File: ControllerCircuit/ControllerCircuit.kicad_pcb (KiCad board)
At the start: 2 copper layers, 122.5 x 87.5 mm, 91 parts, among them J1 ScrewTerminal, J10 Conn_01x02_Female, J11 Conn_01x03_Female, J12 ScrewTerminal, J13 Conn_01x02_Female, J2 ScrewTerminal3Pin, J3 ScrewTerminal3Pin, J4 ScrewTerminal, J5 ScrewTerminal, J6 AVR-ISP-6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

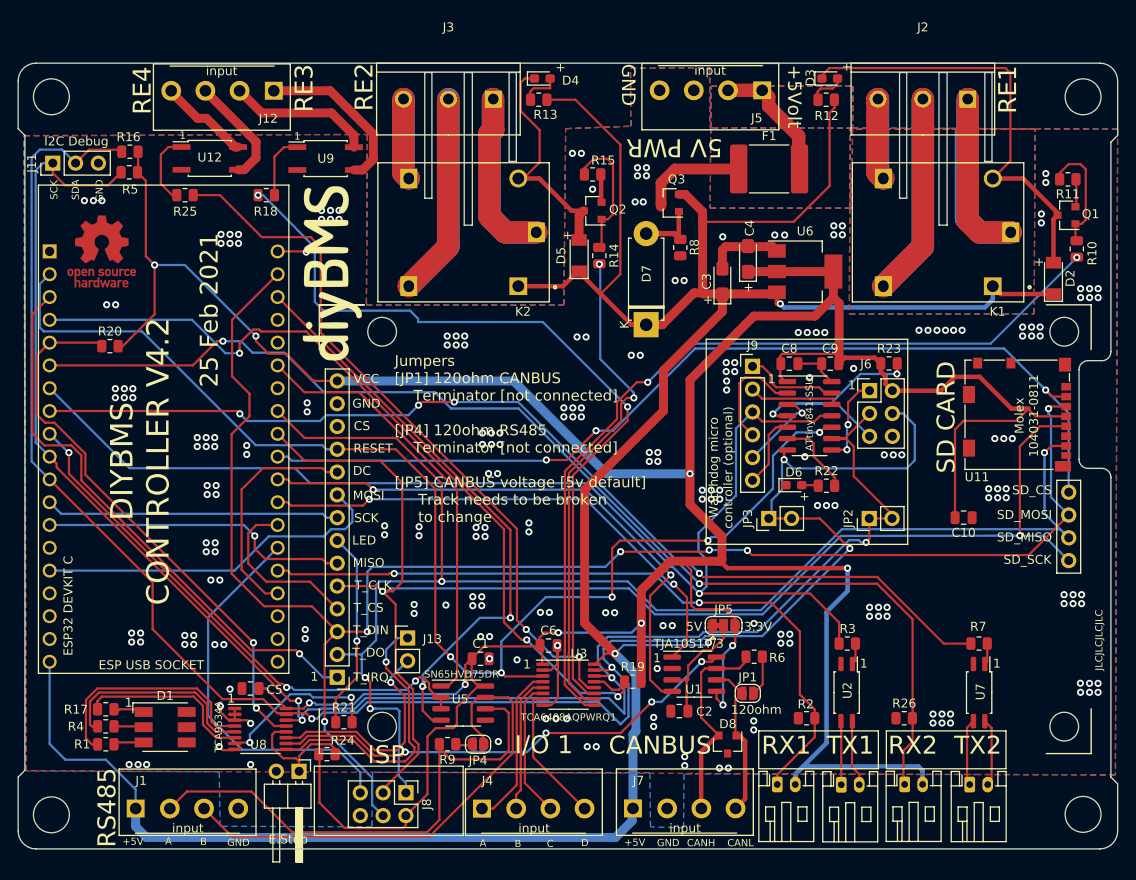
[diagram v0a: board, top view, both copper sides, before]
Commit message: Add pull up to J13 for remote touch display
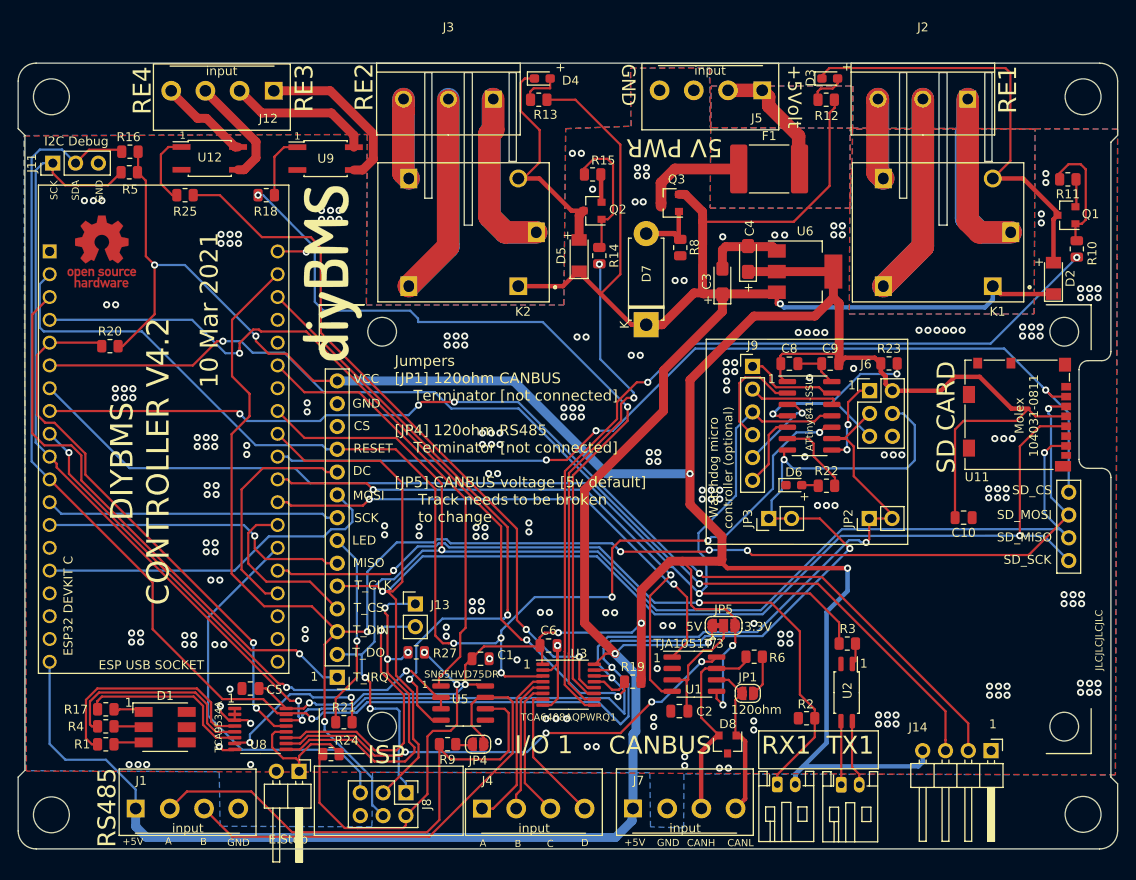
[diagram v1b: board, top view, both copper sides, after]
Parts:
- removed R26: 2K2, Resistor_SMD:R_0805_2012Metric
- removed R7: 180R, Resistor_SMD:R_0805_2012Metric
- removed TX2: Transmit, Connector_JST:JST_PH_S2B-PH-K_1x02_P2.00mm_Horizontal
- removed U7: EL3H7(B)(TA)-G, Package_SO:SOP-4_4.4x2.6mm_P1.27mm
- added R27: 10K, Resistor_SMD:R_0805_2012Metric, F.Cu at (133.1, 116.1)
- J14: renamed from RX2; footprint Connector_JST:JST_PH_S2B-PH-K_1x02_P2.00mm_Horizontal -> Connector_PinHeader_2.54mm:PinHeader_1x04_P2.54mm_Horizontal
- moved J14 10.3 mm to (197.2, 127.0), turned to 270 degrees
- moved J13 3.90 mm to (133.0, 110.7)
- moved R24 0.45 mm to (123.6, 127.4)
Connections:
- J14 pad 1: /IO35_INPUT -> GND
- J14 pad 2: +3V3 -> /IO33
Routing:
- net Net-(J13-Pad1): track 31.7 -> 39.7 mm, vias 1 -> 3
- net Net-(TX2-Pad2): track 7.56 -> 0.00 mm
- net Net-(TX2-Pad1): track 7.48 -> 0.00 mm
- net Net-(J13-Pad2): track 25.1 -> 32.1 mm
- net /IO35_INPUT: track 129.0 -> 122.4 mm
- net /IO33: track 115.1 -> 121.6 mm
- net /VSPI_CLK: track 159.5 -> 162.8 mm
- net +3V3: track 410.5 -> 413.7 mm, vias 10 -> 12
- net /IO22: track 65.4 -> 68.3 mm
- net /IO2: track 80.5 -> 83.3 mm
- net Net-(R7-Pad1): track 2.38 -> 0.00 mm
- net /VSPI_MOSI: track 181.4 -> 182.6 mm
- net /RESET: track 144.2 -> 143.4 mm, vias 5 -> 6
- net /VSPI_MISO: track 159.5 -> 158.9 mm
- net GND: vias 238 -> 235
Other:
- board text added: "10 Mar 2021"
- board text removed: "25 Feb 2021"

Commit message: Added push button switch to wake TFT
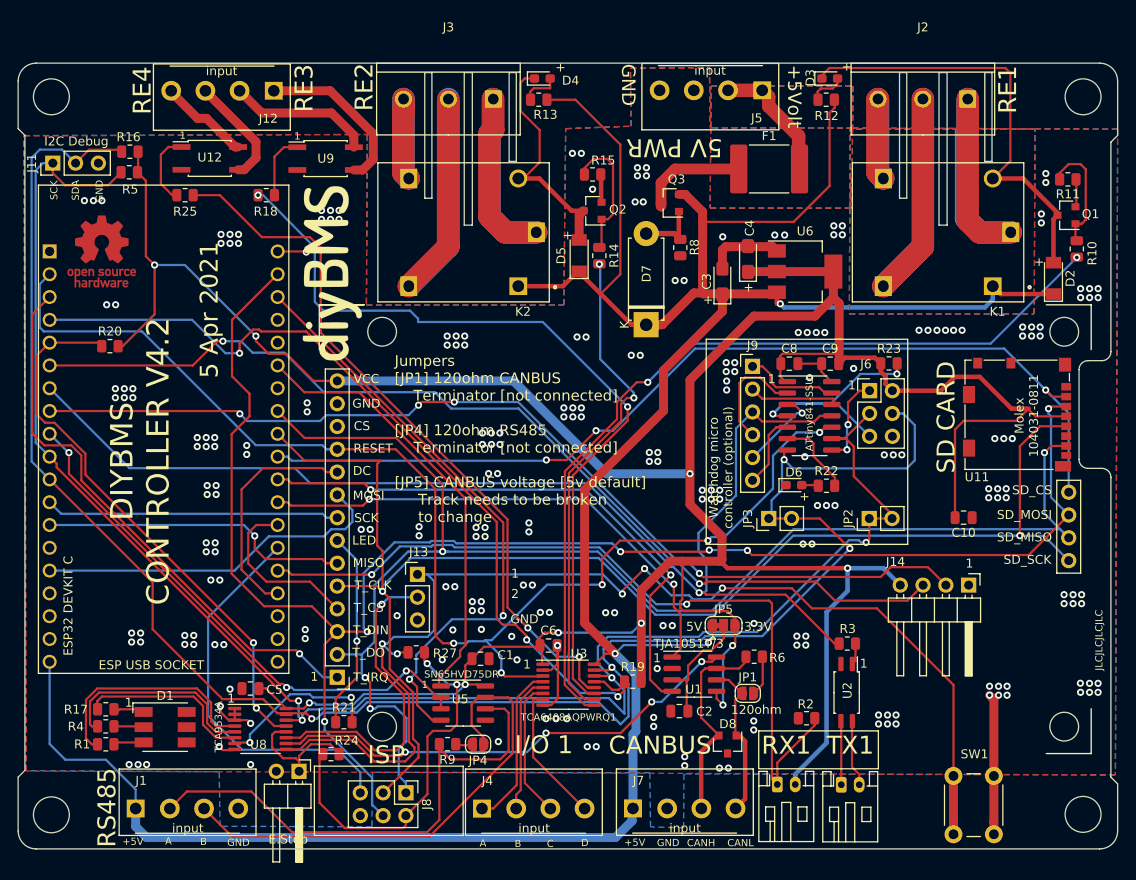
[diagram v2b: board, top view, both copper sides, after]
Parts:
- added SW1: PTS645SL50-2LFS, Button_Switch_THT:SW_PUSH_6mm_H4.3mm, F.Cu at (193.0, 136.4)
- J13: value Conn_01x02_Female -> Conn_01x03_Female; footprint Connector_PinHeader_2.54mm:PinHeader_1x02_P2.54mm_Vertical -> Connector_PinHeader_2.54mm:PinHeader_1x03_P2.54mm_Vertical
- moved J14 18.6 mm to (194.7, 108.6)
- moved J13 3.30 mm to (133.2, 107.4)
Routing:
- net Net-(J13-Pad1): track 39.7 -> 131.0 mm, vias 3 -> 5
- net GND: track 44.9 -> 60.6 mm, vias 235 -> 243
- net /IO35_INPUT: track 122.4 -> 111.3 mm
- net /IO33: track 121.6 -> 110.5 mm
- net +3V3: track 413.7 -> 404.8 mm
- net /IO2: track 83.3 -> 89.2 mm
- net Net-(J13-Pad2): track 32.1 -> 35.8 mm
- net /VSPI_CLK: track 162.8 -> 160.5 mm
- net /RESET: track 143.4 -> 141.9 mm, vias 6 -> 5
- net /IO22: track 68.3 -> 67.0 mm
- net /IO32: track 134.3 -> 133.2 mm
- net /VSPI_MISO: track 158.9 -> 160.0 mm
- net /CANBUS_TX: track 57.9 -> 57.3 mm
- net /IO39_INPUT: track 95.8 -> 96.3 mm
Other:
- board text added: "2"
- board text added: "5 Apr 2021"
- board text removed: "10 Mar 2021"
